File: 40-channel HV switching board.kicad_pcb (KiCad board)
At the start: 2 copper layers, 84 x 96 mm, 194 parts, among them IC1 ATMEGA328P-A, P1 CONN_01X06, P2 CONN_01X06, P3 CONN_02X25, U1 74HC595A, U2 74HC595A, U3 74HC595A, U4 74HC595A, U5 74HC595A, U6 W25Q64FV, Y1 RESONATOR

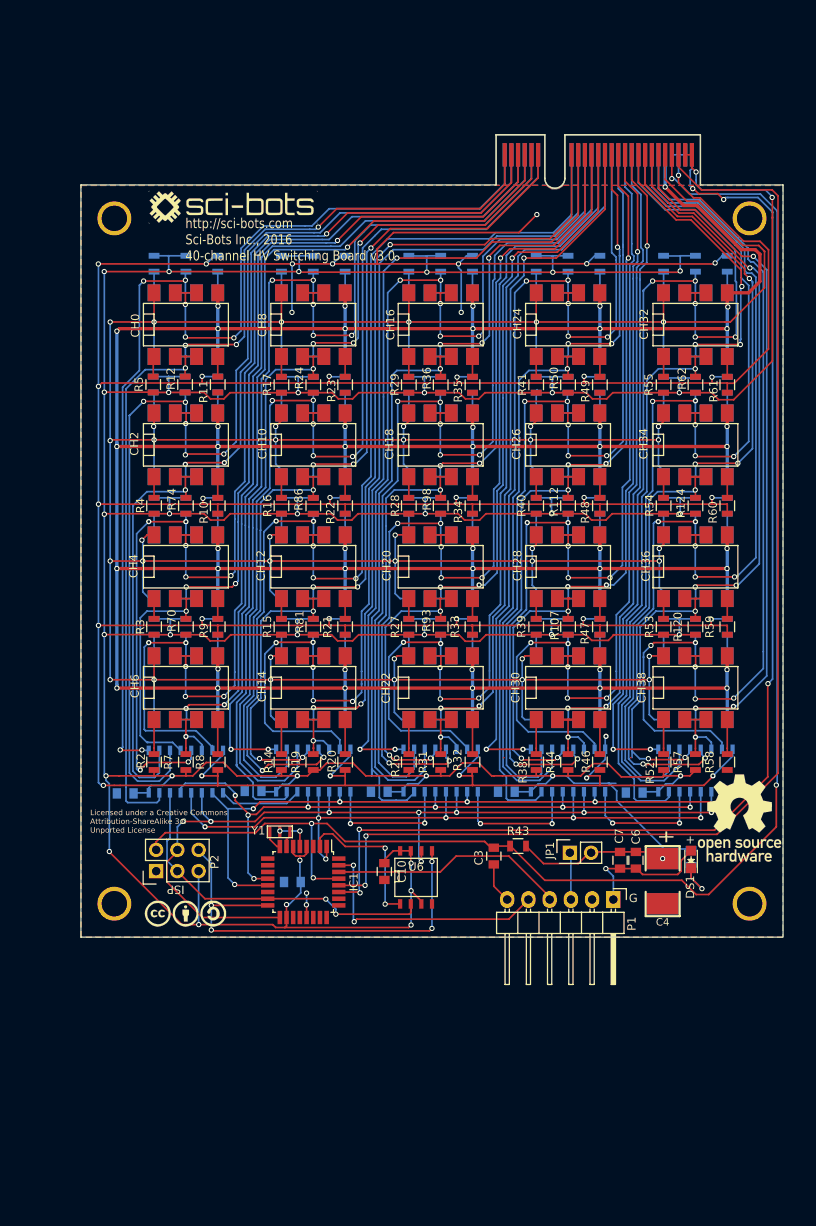
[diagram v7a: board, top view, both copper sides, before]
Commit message: [WIP] Improved layout for EMC
* ground mounting holes
* Add 3.3V and GND power planes
* use solder jumper instead of header pins
* replace edge connector
* extend length of board
* move programming header so that it doesn't extend past the edge of the board
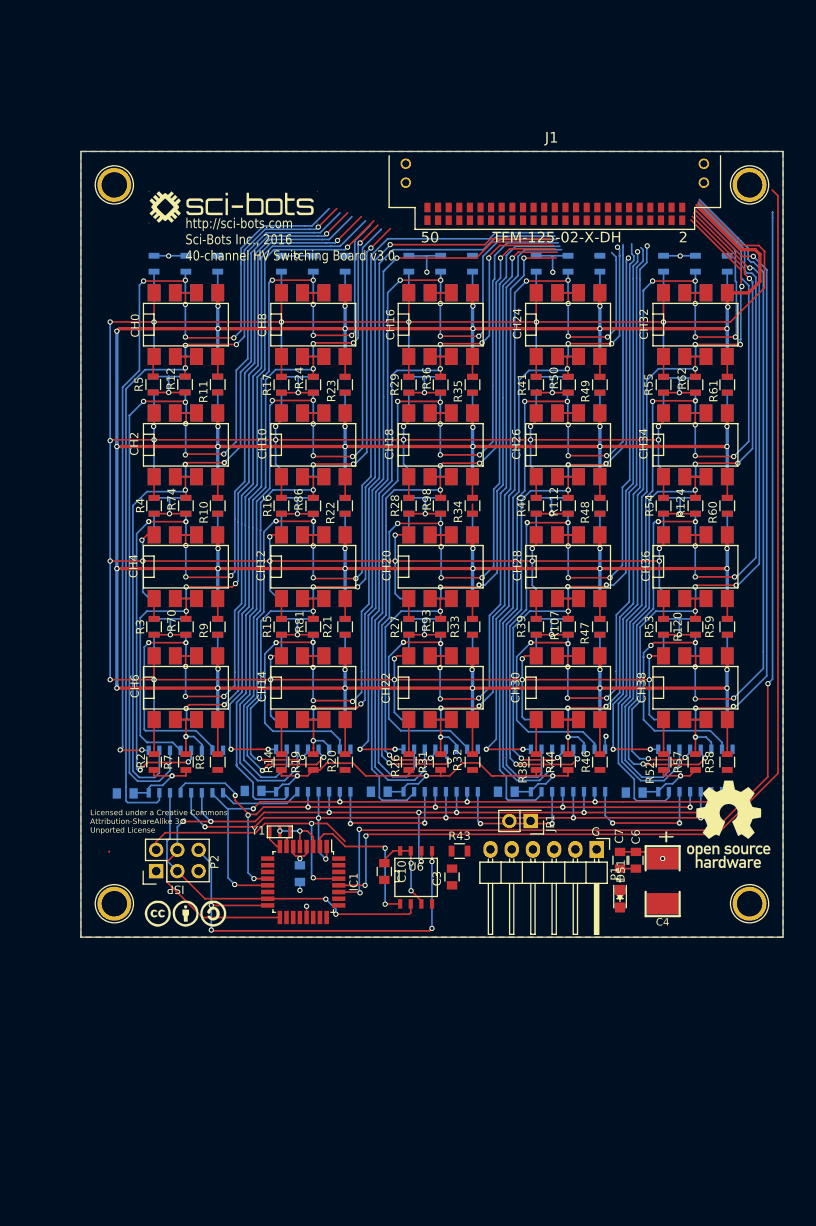
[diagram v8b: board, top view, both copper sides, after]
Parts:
- removed 1PIN (x4): P***, 1pin
- added J1: TFM-125-02-X-DH, WheelerLab:TFM-125-02-X-DH, F.Cu at (80.7, 23.0)
- added P4: CONN_01X01, Connect:1pin, F.Cu at (104.0, 27.0)
- added P5: CONN_01X01, Connect:1pin, F.Cu at (28.0, 113.0)
- added P6: CONN_01X01, Connect:1pin, F.Cu at (104.0, 113.0)
- P3: value CONN_02X25 -> CONN_01X01; footprint WheelerLab:HSEC8-125-XX-X-RA-MATE -> Connect:1pin
- moved P3 52.7 mm to (28.0, 27.0)
- moved R45 9.86 mm to (88.5, 112.4)
- moved DS1 9.71 mm to (88.5, 112.4), turned to 270 degrees
- moved R43 7.03 mm to (69.3, 106.7)
- moved P1 6.32 mm to (85.7, 106.5)
- moved JP1 6.04 mm to (77.8, 103.1), turned to 180 degrees
- moved C3 5.59 mm to (68.4, 109.8)
- moved G*** 1.50 mm to (101.5, 103.5)
- moved C13 1.35 mm to (50.2, 109.4), turned to 90 degrees
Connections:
- DS1 pad 1: Net-(DS1-Pad1) -> GND
- DS1 pad 2: GND -> Net-(DS1-Pad2)
- P3 pad 1: HVOUT0 -> GND
- R45 pad 2: Net-(DS1-Pad1) -> Net-(DS1-Pad2)
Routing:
- net GND: track 631.1 -> 17.2 mm, vias 41 -> 5
- net +3.3V: track 745.7 -> 268.3 mm, vias 40 -> 29
- net RST: track 183.6 -> 35.0 mm, vias 4 -> 2
- net RX: track 30.5 -> 0.00 mm, vias 2 -> 0
- net TX: track 28.4 -> 0.00 mm
- net HVOUT0: track 62.9 -> 37.2 mm
- net HVOUT2: track 75.9 -> 50.6 mm
- net HVOUT1: track 59.8 -> 35.0 mm
- net HVOUT4: track 91.1 -> 66.2 mm
- net HVOUT3: track 73.3 -> 48.8 mm
- net HVOUT8: track 50.8 -> 26.4 mm
- net HVOUT6: track 105.1 -> 81.0 mm
- net HVOUT10: track 65.1 -> 41.1 mm
- net HVOUT5: track 88.5 -> 64.8 mm
- net HVOUT9: track 47.8 -> 24.2 mm
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- added copper zone on 3.3V, net +3.3V
- added copper zone on GND, net GND
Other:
- board size 84 x 96 mm -> 84 x 94 mm
- copper layers 2 -> 4
